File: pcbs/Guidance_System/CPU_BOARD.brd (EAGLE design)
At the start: 100 x 52.1 mm, 29 parts, among them J1 22-27-2081-08, J10 22-27-2081-08, J11 22-27-2081-08, J12 22-27-2081-08, J13 22-27-2081-08, J14 22-27-2081-08, J15 22-27-2041-04, J16 22-27-2041-04, J17 22-27-2021-02, J2 22-27-2021-02, J3 22-27-2041-04, J4 22-27-2041-04, J5 22-27-2081-08, J6 22-27-2021-02, J7 22-27-2081-08, J8 22-27-2021-02, J9 22-27-2021-02

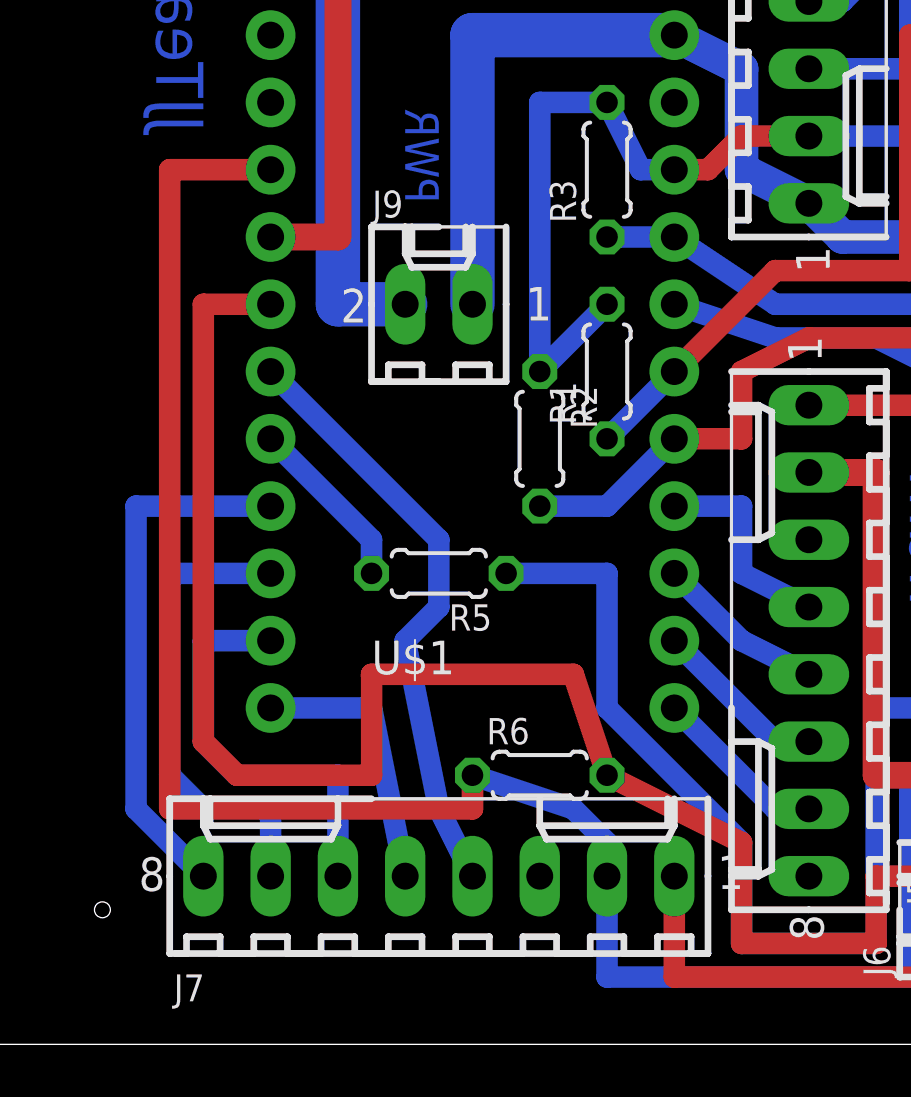
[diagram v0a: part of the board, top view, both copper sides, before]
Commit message: * Re-org'd tracks. Looks tidier
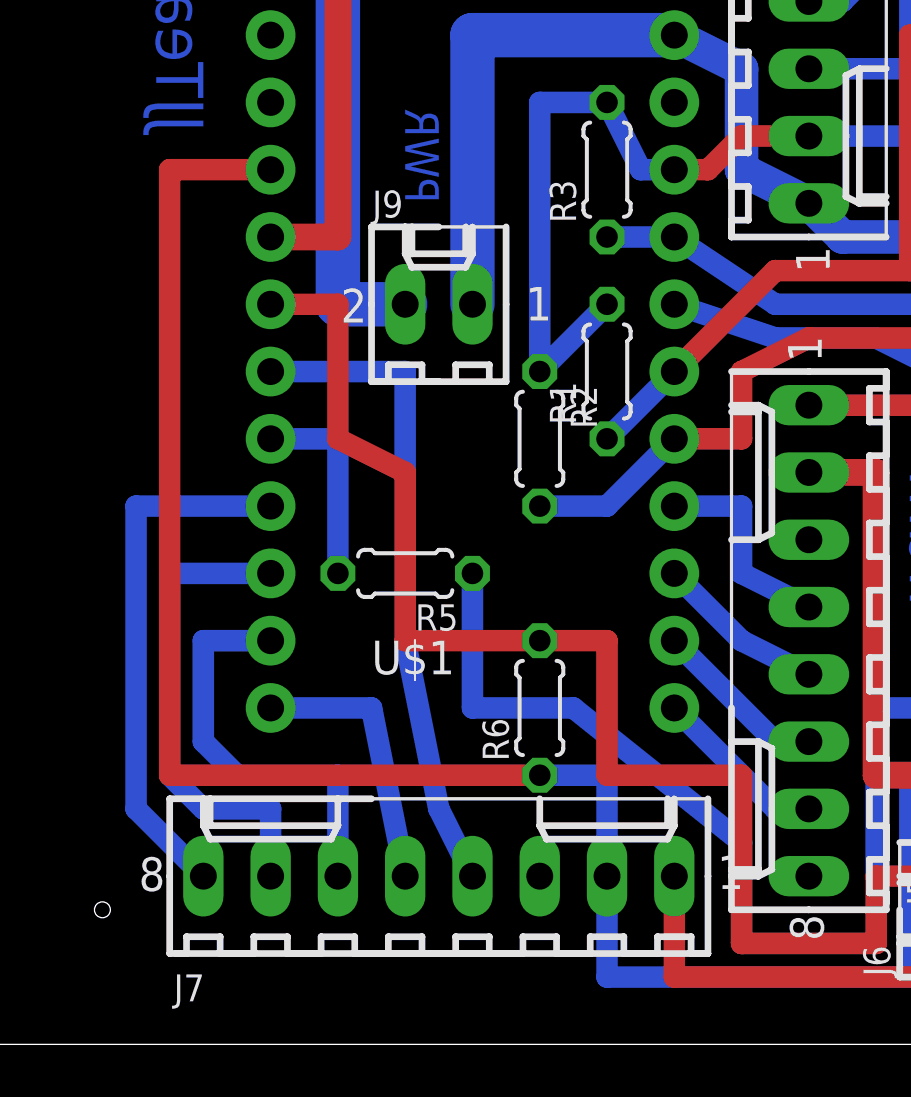
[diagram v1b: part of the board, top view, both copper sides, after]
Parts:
- moved R6 2.54 mm to (73.7, 38.1), turned to 90 degrees
- moved R5 1.27 mm to (68.6, 43.2)
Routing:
- net N$17: track 62.3 -> 52.4 mm
- net N$23: track 22.6 -> 24.6 mm
- net N$15: track 6.66 -> 7.62 mm
- net N$16: track 38.9 -> 39.9 mm
- net GND: track 93.4 -> 92.7 mm
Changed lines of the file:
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@@
 <element name="R3" library="rcl" package="0204/5" value="" x="76.2" y="58.42" rot="R90"/>
 <element name="R4" library="rcl" package="0204/5" value="" x="92.71" y="44.45" rot="R90"/>
-<element name="R5" library="resistor" package="0204/5" value="" x="69.85" y="43.18" rot="R180"/>
-<element name="R6" library="rcl" package="0204/5" value="" x="73.66" y="35.56"/>
+<element name="R5" library="resistor" package="0204/5" value="" x="68.58" y="43.18" rot="R180"/>
+<element name="R6" library="rcl" package="0204/5" value="" x="73.66" y="38.1" rot="R90"/>
 <element name="U$1" library="Joe_SparkFun-Boards" package="ARDUINO_MINI" value="ARDUINO_MINI" x="71.12" y="53.34"/>
 <element name="J8" library="con-molex" package="6410-02" value="22-27-2021-02" x="69.85" y="72.39" rot="R180">
@@
 <contactref element="J7" pad="2"/>
 <contactref element="J5" pad="2"/>
-<wire x1="76.2" y1="31.75" x2="76.2" y2="33.02" width="0.8128" layer="16"/>
-<wire x1="76.2" y1="33.02" x2="74.93" y2="34.29" width="0.8128" layer="16"/>
-<wire x1="74.93" y1="34.29" x2="71.12" y2="35.56" width="0.8128" layer="16"/>
+<wire x1="76.2" y1="31.75" x2="76.2" y2="35.56" width="0.8128" layer="16"/>
+<wire x1="76.2" y1="35.56" x2="73.66" y2="35.56" width="0.8128" layer="16"/>
 <wire x1="87.63" y1="27.94" x2="76.2" y2="27.94" width="0.8128" layer="16"/>
 <wire x1="76.2" y1="27.94" x2="76.2" y2="31.75" width="0.8128" layer="16"/>
 <wire x1="63.5" y1="58.42" x2="59.69" y2="58.42" width="0.8128" layer="1"/>
-<wire x1="59.69" y1="58.42" x2="59.69" y2="34.29" width="0.8128" layer="1"/>
-<wire x1="59.69" y1="34.29" x2="71.12" y2="34.29" width="0.8128" layer="1"/>
-<wire x1="71.12" y1="34.29" x2="71.12" y2="35.56" width="0.8128" layer="1"/>
+<wire x1="59.69" y1="58.42" x2="59.69" y2="35.56" width="0.8128" layer="1"/>
+<wire x1="59.69" y1="35.56" x2="73.66" y2="35.56" width="0.8128" layer="1"/>
 <wire x1="83.82" y1="46.99" x2="86.36" y2="46.99" width="1.016" layer="1"/>
 <wire x1="86.36" y1="46.99" x2="86.36" y2="35.56" width="1.016" layer="1"/>
@@
 <contactref element="U$1" pad="8"/>
 <contactref element="R5" pad="2"/>
-<wire x1="63.5" y1="48.26" x2="67.31" y2="44.45" width="0.8128" layer="16"/>
-<wire x1="67.31" y1="44.45" x2="67.31" y2="43.18" width="0.8128" layer="16"/>
+<wire x1="63.5" y1="48.26" x2="66.04" y2="48.26" width="0.8128" layer="16"/>
+<wire x1="66.04" y1="48.26" x2="66.04" y2="43.18" width="0.8128" layer="16"/>
 </signal>
 <signal name="N$16">
 <contactref element="R5" pad="1"/>
 <contactref element="LED1" pad="A"/>
-<wire x1="72.39" y1="43.18" x2="76.2" y2="43.18" width="0.8128" layer="16"/>
-<wire x1="76.2" y1="43.18" x2="76.2" y2="38.1" width="0.8128" layer="16"/>
-<wire x1="76.2" y1="38.1" x2="81.28" y2="33.02" width="0.8128" layer="16"/>
+<wire x1="71.12" y1="43.18" x2="71.12" y2="38.1" width="0.8128" layer="16"/>
+<wire x1="71.12" y1="38.1" x2="74.93" y2="38.1" width="0.8128" layer="16"/>
+<wire x1="74.93" y1="38.1" x2="81.28" y2="33.02" width="0.8128" layer="16"/>
 <wire x1="81.28" y1="33.02" x2="81.28" y2="29.21" width="0.8128" layer="16"/>
 <wire x1="81.28" y1="29.21" x2="86.36" y2="29.21" width="0.8128" layer="16"/>
@@
 <contactref element="R6" pad="2"/>
 <contactref element="J6" pad="1"/>
-<wire x1="63.5" y1="53.34" x2="60.96" y2="53.34" width="0.8128" layer="1"/>
-<wire x1="60.96" y1="53.34" x2="60.96" y2="36.83" width="0.8128" layer="1"/>
-<wire x1="60.96" y1="36.83" x2="62.23" y2="35.56" width="0.8128" layer="1"/>
-<wire x1="62.23" y1="35.56" x2="67.31" y2="35.56" width="0.8128" layer="1"/>
-<wire x1="67.31" y1="35.56" x2="67.31" y2="39.37" width="0.8128" layer="1"/>
-<wire x1="67.31" y1="39.37" x2="74.93" y2="39.37" width="0.8128" layer="1"/>
-<wire x1="74.93" y1="39.37" x2="76.2" y2="35.56" width="0.8128" layer="1"/>
-<wire x1="76.2" y1="35.56" x2="81.28" y2="33.02" width="0.8128" layer="1"/>
-<wire x1="81.28" y1="33.02" x2="81.28" y2="29.21" width="0.8128" layer="1"/>
+<wire x1="63.5" y1="53.34" x2="66.04" y2="53.34" width="0.8128" layer="1"/>
+<wire x1="66.04" y1="53.34" x2="66.04" y2="48.26" width="0.8128" layer="1"/>
+<wire x1="66.04" y1="48.26" x2="68.58" y2="46.99" width="0.8128" layer="1"/>
+<wire x1="68.58" y1="46.99" x2="68.58" y2="40.64" width="0.8128" layer="1"/>
+<wire x1="68.58" y1="40.64" x2="73.66" y2="40.64" width="0.8128" layer="1"/>
+<wire x1="73.66" y1="40.64" x2="76.2" y2="40.64" width="0.8128" layer="1"/>
+<wire x1="76.2" y1="40.64" x2="76.2" y2="35.56" width="0.8128" layer="1"/>
+<wire x1="76.2" y1="35.56" x2="81.28" y2="35.56" width="0.8128" layer="1"/>
+<wire x1="81.28" y1="35.56" x2="81.28" y2="29.21" width="0.8128" layer="1"/>
 <wire x1="81.28" y1="29.21" x2="86.36" y2="29.21" width="0.8128" layer="1"/>
 <wire x1="86.36" y1="29.21" x2="86.36" y2="31.75" width="0.8128" layer="1"/>
@@
 <contactref element="U$1" pad="7"/>
 <contactref element="J7" pad="4"/>
-<wire x1="63.5" y1="50.8" x2="69.85" y2="44.45" width="0.8128" layer="16"/>
-<wire x1="69.85" y1="44.45" x2="69.85" y2="41.91" width="0.8128" layer="16"/>
-<wire x1="69.85" y1="41.91" x2="68.58" y2="40.64" width="0.8128" layer="16"/>
+<wire x1="63.5" y1="50.8" x2="68.58" y2="50.8" width="0.8128" layer="16"/>
+<wire x1="68.58" y1="50.8" x2="68.58" y2="40.64" width="0.8128" layer="16"/>
 <wire x1="68.58" y1="40.64" x2="69.85" y2="34.29" width="0.8128" layer="16"/>
 <wire x1="69.85" y1="34.29" x2="71.12" y2="31.75" width="0.8128" layer="16"/>

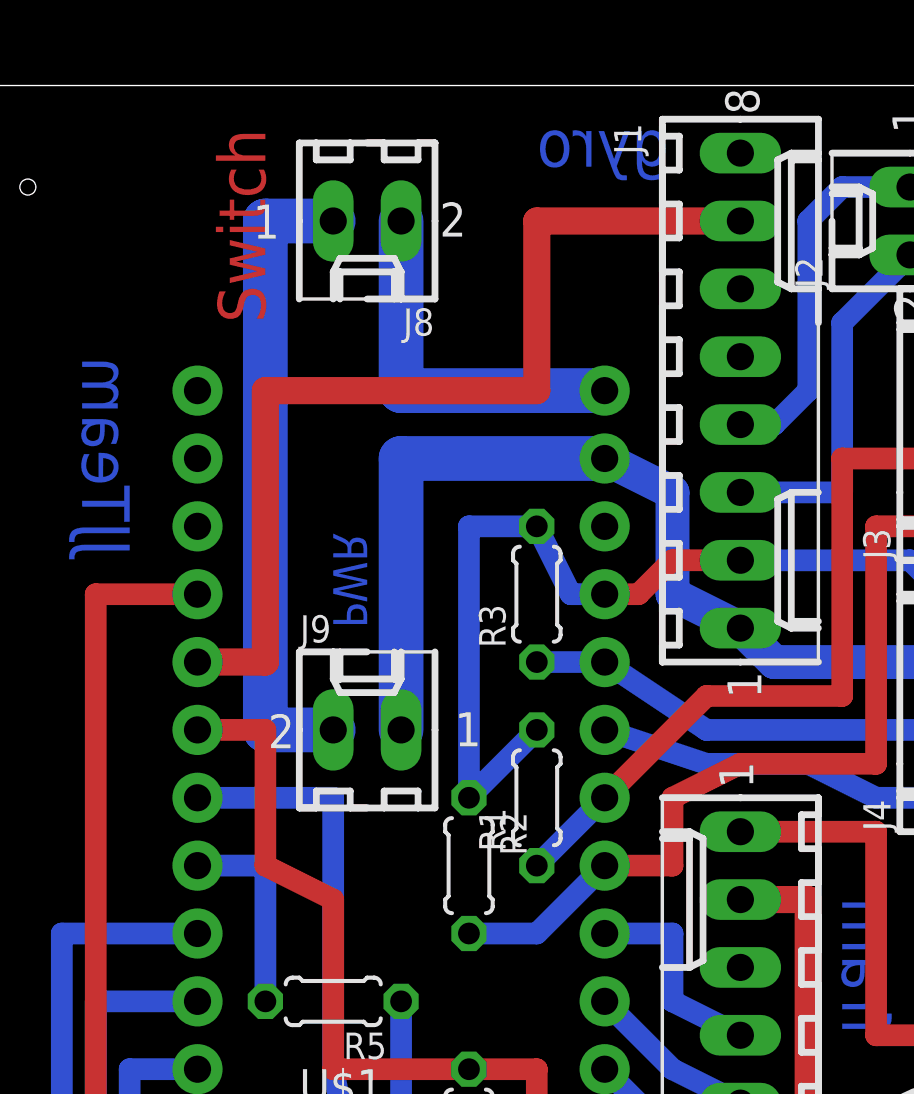
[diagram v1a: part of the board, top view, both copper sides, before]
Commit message: * Adding in resistors, so we can measure voltage of battery at some point.
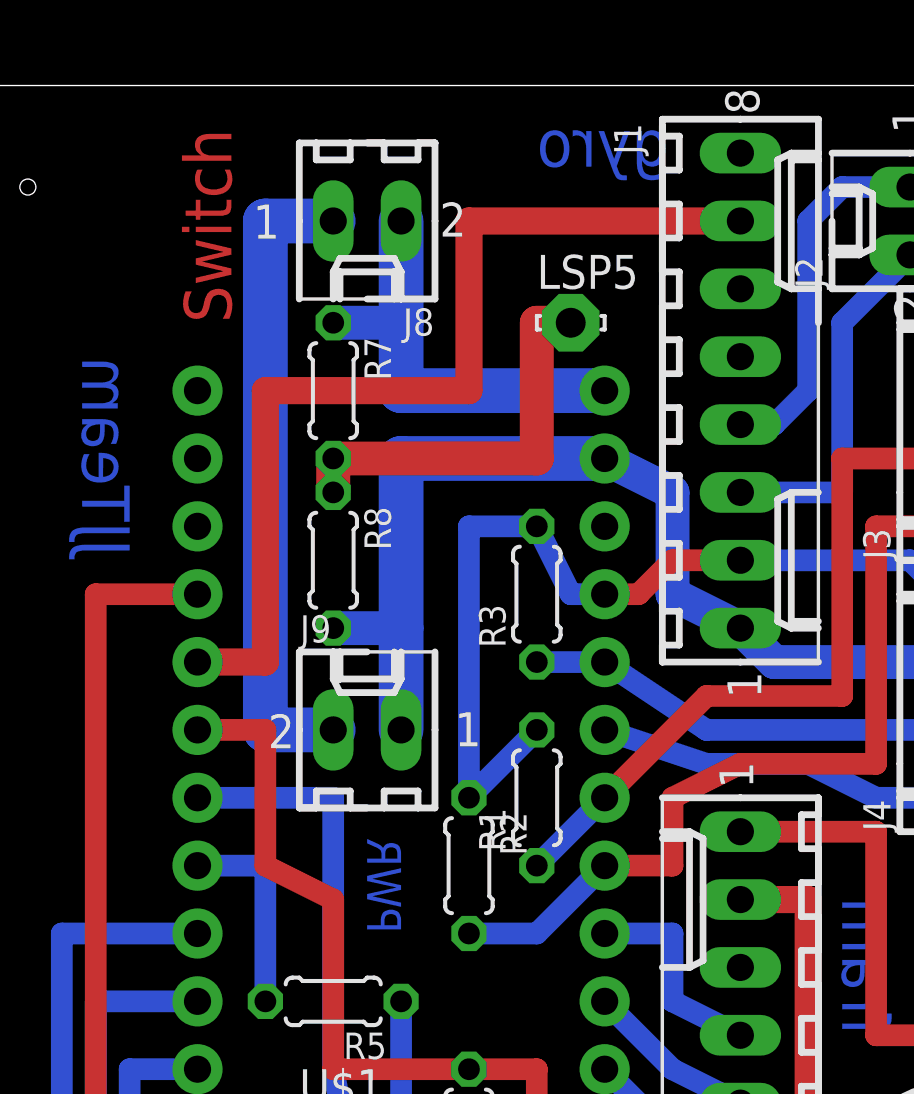
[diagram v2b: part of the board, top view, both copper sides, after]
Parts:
- added LSP5: LSP11, solpad:LSP11
- added R7, R8: (no value), rcl:0204/5
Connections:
- new net N$47: LSP5.MP, R7.2, R8.1
- net N$24: now also R8.2
- net N$5: now also R7.1
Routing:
- net N$47: track 0.00 -> 15.2 mm
- net N$5: track 14.0 -> 16.5 mm
- net N$24: track 51.2 -> 53.7 mm
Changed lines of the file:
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@@
 <text x="99.06" y="59.69" size="1.778" layer="1" rot="R90">S1 Sense</text>
 <text x="99.06" y="48.26" size="1.778" layer="1" rot="R90">S2 Sense</text>
-<text x="68.58" y="57.15" size="1.27" layer="16" rot="MR90">PWR</text>
-<text x="66.04" y="68.58" size="1.778" layer="1" rot="R90">Switch</text>
+<text x="69.85" y="45.72" size="1.27" layer="16" rot="MR90">PWR</text>
+<text x="64.77" y="68.58" size="1.778" layer="1" rot="R90">Switch</text>
 <text x="95.25" y="71.12" size="1.778" layer="1" rot="R90">i2c</text>
 <text x="99.06" y="35.56" size="1.778" layer="1" rot="R90">Status</text>
@@
 <element name="LSP3" library="solpad" package="LSP10" value="LSP10" x="16.51" y="62.23"/>
 <element name="LSP4" library="solpad" package="LSP10" value="LSP10" x="21.59" y="62.23"/>
+<element name="R7" library="rcl" package="0204/5" value="" x="68.58" y="66.04" rot="R270"/>
+<element name="R8" library="rcl" package="0204/5" value="" x="68.58" y="59.69" rot="R270"/>
+<element name="LSP5" library="solpad" package="LSP11" value="LSP11" x="77.47" y="68.58"/>
 </elements>
 <signals>
@@
 <contactref element="U$1" pad="24"/>
 <contactref element="J8" pad="2"/>
-<wire x1="71.12" y1="72.39" x2="71.12" y2="66.04" width="1.6764" layer="16"/>
+<wire x1="71.12" y1="72.39" x2="71.12" y2="68.58" width="1.6764" layer="16"/>
+<wire x1="71.12" y1="68.58" x2="71.12" y2="66.04" width="1.6764" layer="16"/>
 <wire x1="71.12" y1="66.04" x2="78.74" y2="66.04" width="1.6764" layer="16"/>
+<contactref element="R7" pad="1"/>
+<wire x1="68.58" y1="68.58" x2="71.12" y2="68.58" width="1.27" layer="16"/>
 </signal>
 <signal name="N$6">
 <contactref element="U$1" pad="5"/>
 <contactref element="J1" pad="7"/>
-<wire x1="83.82" y1="72.39" x2="76.2" y2="72.39" width="1.016" layer="1"/>
-<wire x1="76.2" y1="72.39" x2="76.2" y2="66.04" width="1.016" layer="1"/>
-<wire x1="76.2" y1="66.04" x2="66.04" y2="66.04" width="1.016" layer="1"/>
+<wire x1="83.82" y1="72.39" x2="73.66" y2="72.39" width="1.016" layer="1"/>
+<wire x1="73.66" y1="72.39" x2="73.66" y2="66.04" width="1.016" layer="1"/>
+<wire x1="73.66" y1="66.04" x2="66.04" y2="66.04" width="1.016" layer="1"/>
 <wire x1="66.04" y1="66.04" x2="66.04" y2="55.88" width="1.016" layer="1"/>
 <wire x1="66.04" y1="55.88" x2="63.5" y2="55.88" width="1.016" layer="1"/>
@@
 <wire x1="92.71" y1="55.88" x2="85.09" y2="55.88" width="1.27" layer="16"/>
 <wire x1="85.09" y1="55.88" x2="83.82" y2="57.15" width="1.27" layer="16"/>
-<wire x1="71.12" y1="53.34" x2="71.12" y2="63.5" width="1.6764" layer="16"/>
+<wire x1="71.12" y1="53.34" x2="71.12" y2="57.15" width="1.6764" layer="16"/>
+<wire x1="71.12" y1="57.15" x2="71.12" y2="63.5" width="1.6764" layer="16"/>
 <wire x1="71.12" y1="63.5" x2="78.74" y2="63.5" width="1.6764" layer="16"/>
 <wire x1="78.74" y1="63.5" x2="81.28" y2="62.23" width="1.27" layer="16"/>
 <wire x1="81.28" y1="62.23" x2="81.28" y2="58.42" width="1.27" layer="16"/>
 <wire x1="81.28" y1="58.42" x2="83.82" y2="57.15" width="1.27" layer="16"/>
+<contactref element="R8" pad="2"/>
+<wire x1="68.58" y1="57.15" x2="71.12" y2="57.15" width="1.27" layer="16"/>
 </signal>
 <signal name="N$4">
@@
 <wire x1="16.51" y1="62.23" x2="16.51" y2="59.69" width="1.016" layer="16"/>
 </signal>
+<signal name="N$47">
+<contactref element="R7" pad="2"/>
+<contactref element="R8" pad="1"/>
+<contactref element="LSP5" pad="MP"/>
+<wire x1="77.47" y1="68.58" x2="76.2" y2="68.58" width="1.27" layer="1"/>
+<wire x1="76.2" y1="68.58" x2="76.2" y2="63.5" width="1.27" layer="1"/>
+<wire x1="76.2" y1="63.5" x2="68.58" y2="63.5" width="1.27" layer="1"/>
+<wire x1="68.58" y1="62.23" x2="68.58" y2="63.5" width="1.27" layer="1"/>
+</signal>
 </signals>

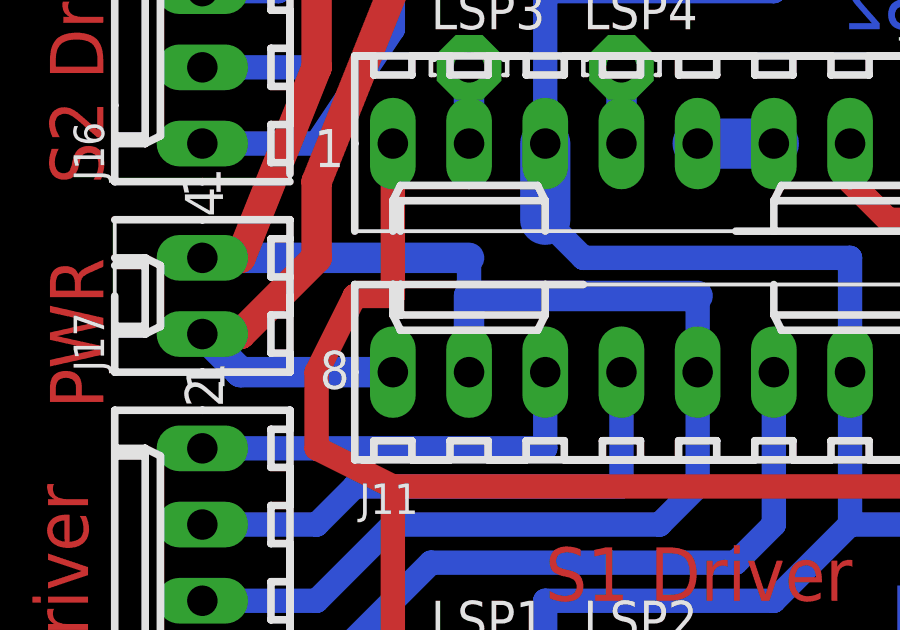
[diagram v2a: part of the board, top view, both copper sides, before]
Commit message: * Fixed bad track that went to wrong pin!
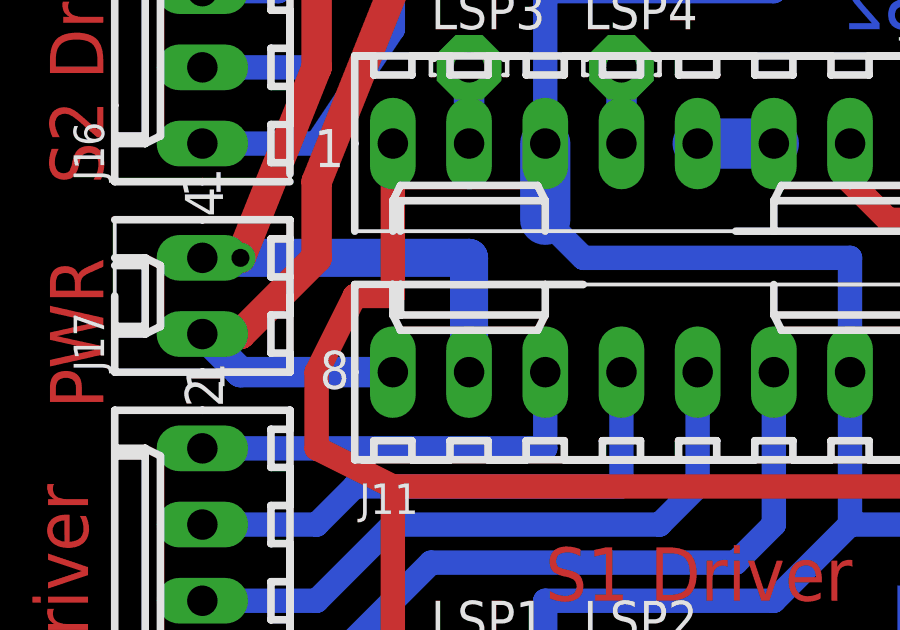
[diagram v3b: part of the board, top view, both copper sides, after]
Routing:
- net N$34: track 51.3 -> 39.9 mm
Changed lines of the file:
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@@
 <contactref element="J11" pad="7"/>
 <contactref element="J17" pad="1"/>
-<via x="24.13" y="52.07" extent="1-16" drill="0.6" shape="square"/>
-<wire x1="7.62" y1="55.88" x2="16.51" y2="55.88" width="1.016" layer="16"/>
-<wire x1="16.51" y1="55.88" x2="16.51" y2="54.61" width="0.8128" layer="16"/>
-<wire x1="16.51" y1="52.07" x2="16.51" y2="54.61" width="1.016" layer="16"/>
-<wire x1="16.51" y1="54.61" x2="24.13" y2="54.61" width="1.016" layer="16"/>
 <wire x1="16.51" y1="72.39" x2="16.51" y2="74.93" width="0.8128" layer="1"/>
 <wire x1="16.51" y1="74.93" x2="11.43" y2="74.93" width="1.016" layer="1"/>
@@
 <wire x1="11.43" y1="62.23" x2="8.89" y2="55.88" width="1.016" layer="1"/>
 <wire x1="8.89" y1="55.88" x2="7.62" y2="55.88" width="1.016" layer="1"/>
-<wire x1="24.13" y1="54.61" x2="24.13" y2="52.07" width="0.8128" layer="16"/>
+<via x="8.89" y="55.88" extent="1-16" drill="0.6" shape="square"/>
+<wire x1="8.89" y1="55.88" x2="16.51" y2="55.88" width="1.27" layer="16"/>
+<wire x1="16.51" y1="55.88" x2="16.51" y2="52.07" width="1.27" layer="16"/>
 </signal>
 <signal name="N$35">
